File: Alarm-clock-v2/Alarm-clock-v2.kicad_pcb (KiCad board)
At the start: 2 copper layers, 51 x 53.5 mm, 23 parts, among them CON1 AVR-ISP-6, J1 USB_OTG, SW1 SW_SPST, SW2 SW_SPST, SW3 SW_SPST, U1 ATMEGA32U4-AU, U2 CA56-12CGKWA, Y1 Crystal

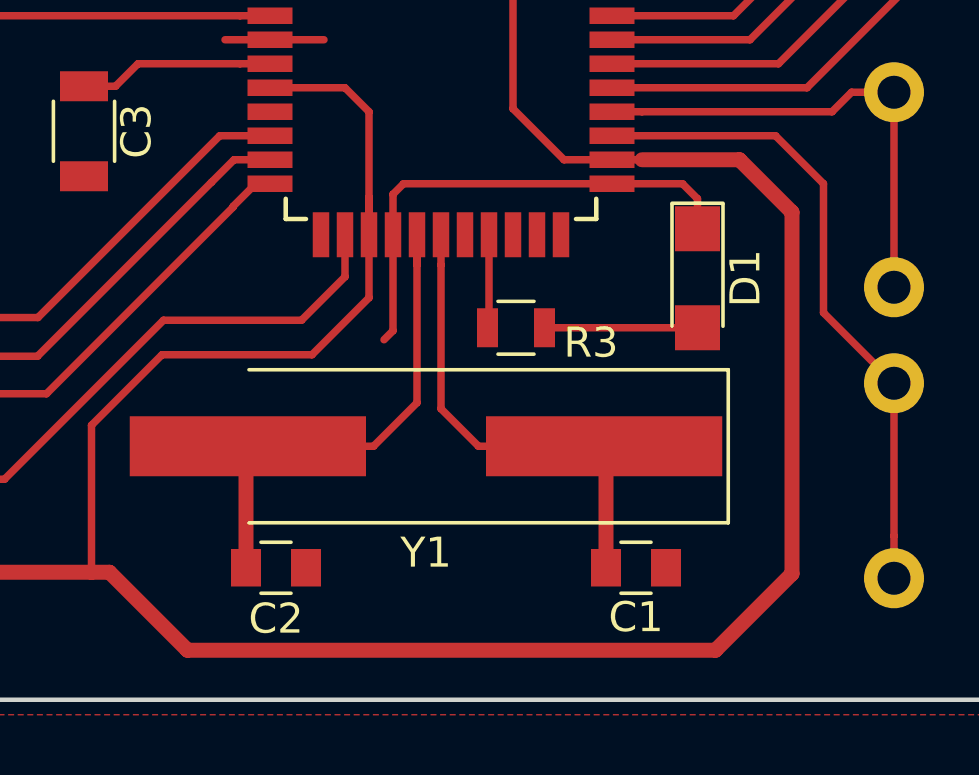
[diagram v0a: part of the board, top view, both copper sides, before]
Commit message: Added buzzer
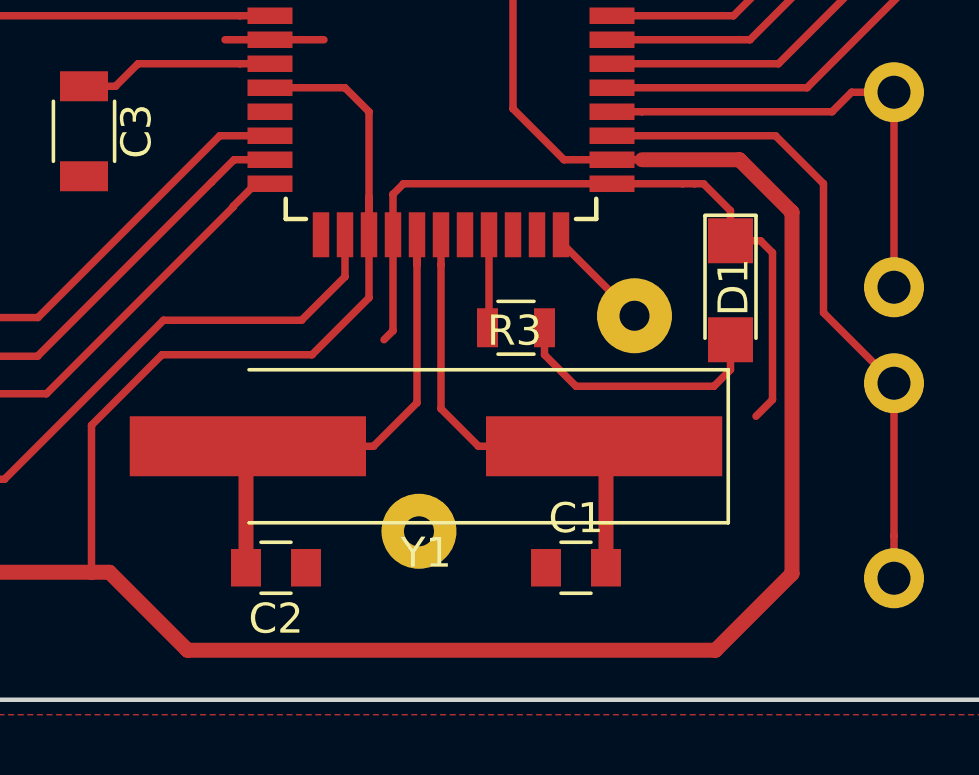
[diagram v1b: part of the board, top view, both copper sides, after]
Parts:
- added BZ1: Buzzer, Buzzers_Beepers:BUZZER, B.Cu at (193.4, 128.8)
- moved C1 2.00 mm to (195.1, 133.6), turned to 180 degrees
- moved D1 1.17 mm to (200.2, 124.3)
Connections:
- U1 pad 22: (no net) -> Net-(BZ1-Pad1)
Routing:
- net GND: track 47.7 -> 56.2 mm
- net Net-(BZ1-Pad1): track 0.00 -> 3.91 mm
- net Net-(D1-Pad2): track 5.10 -> 8.76 mm
